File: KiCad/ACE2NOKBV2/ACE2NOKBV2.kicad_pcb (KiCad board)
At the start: 2 copper layers, 160 x 100 mm, 107 parts, among them IC1 78T, IC2 74367N, Q1 2N3904, Q2 2N3904, Q3 BC237, X1 6.556MHz

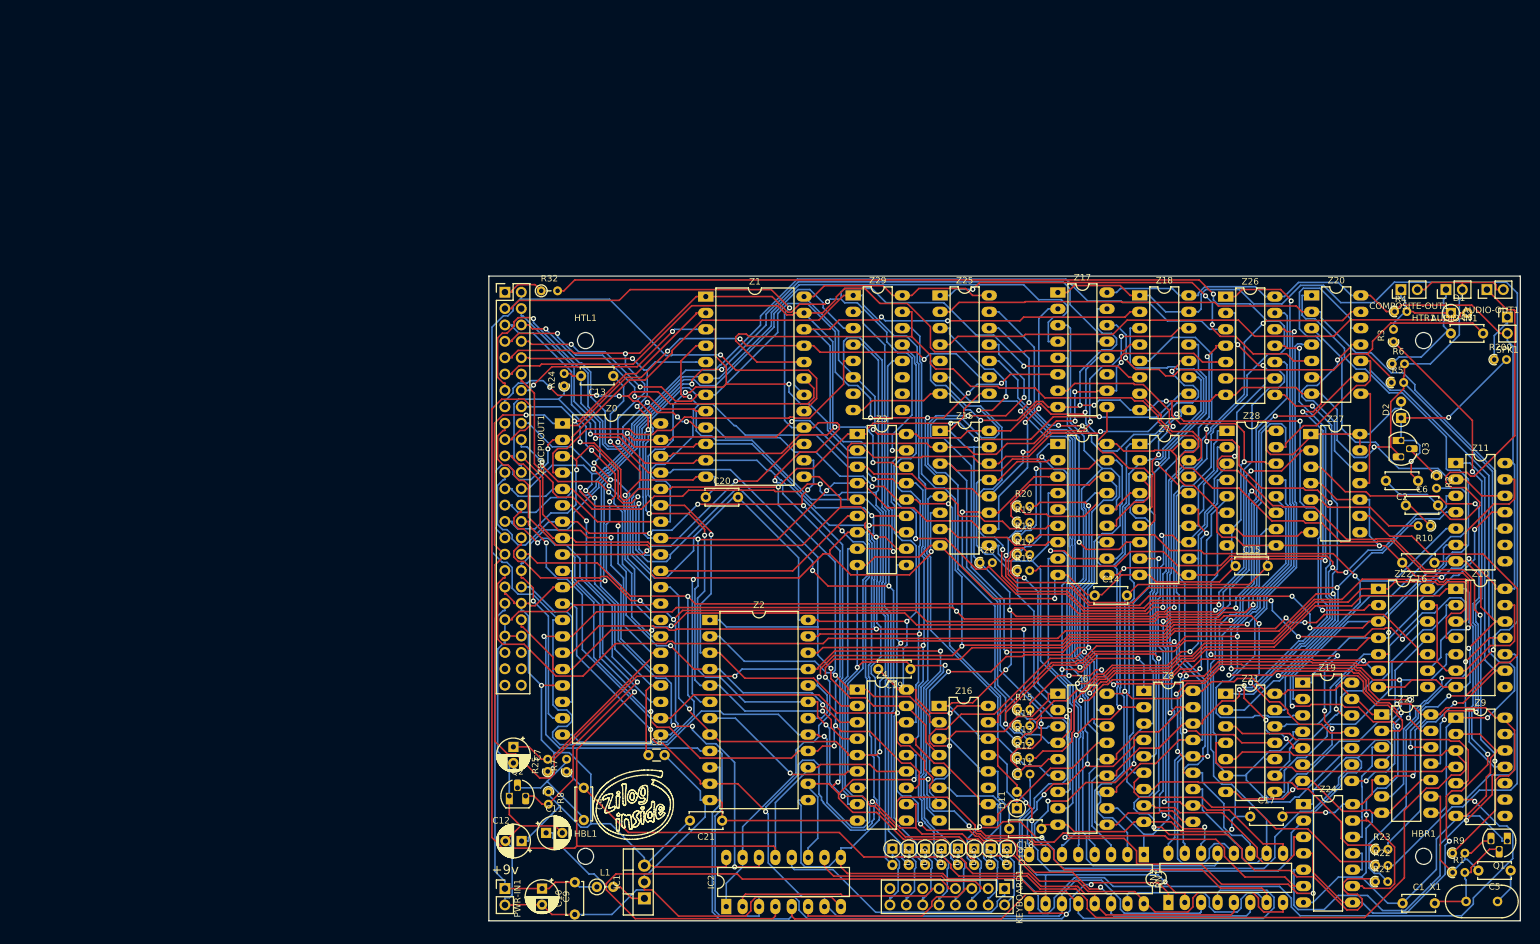
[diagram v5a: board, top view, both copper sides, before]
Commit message: Remove Speakrer leave 2 pin connector add single transistor amp to composite out.
Signed-off-by: John Bradley <flypie@rocketmail.com>
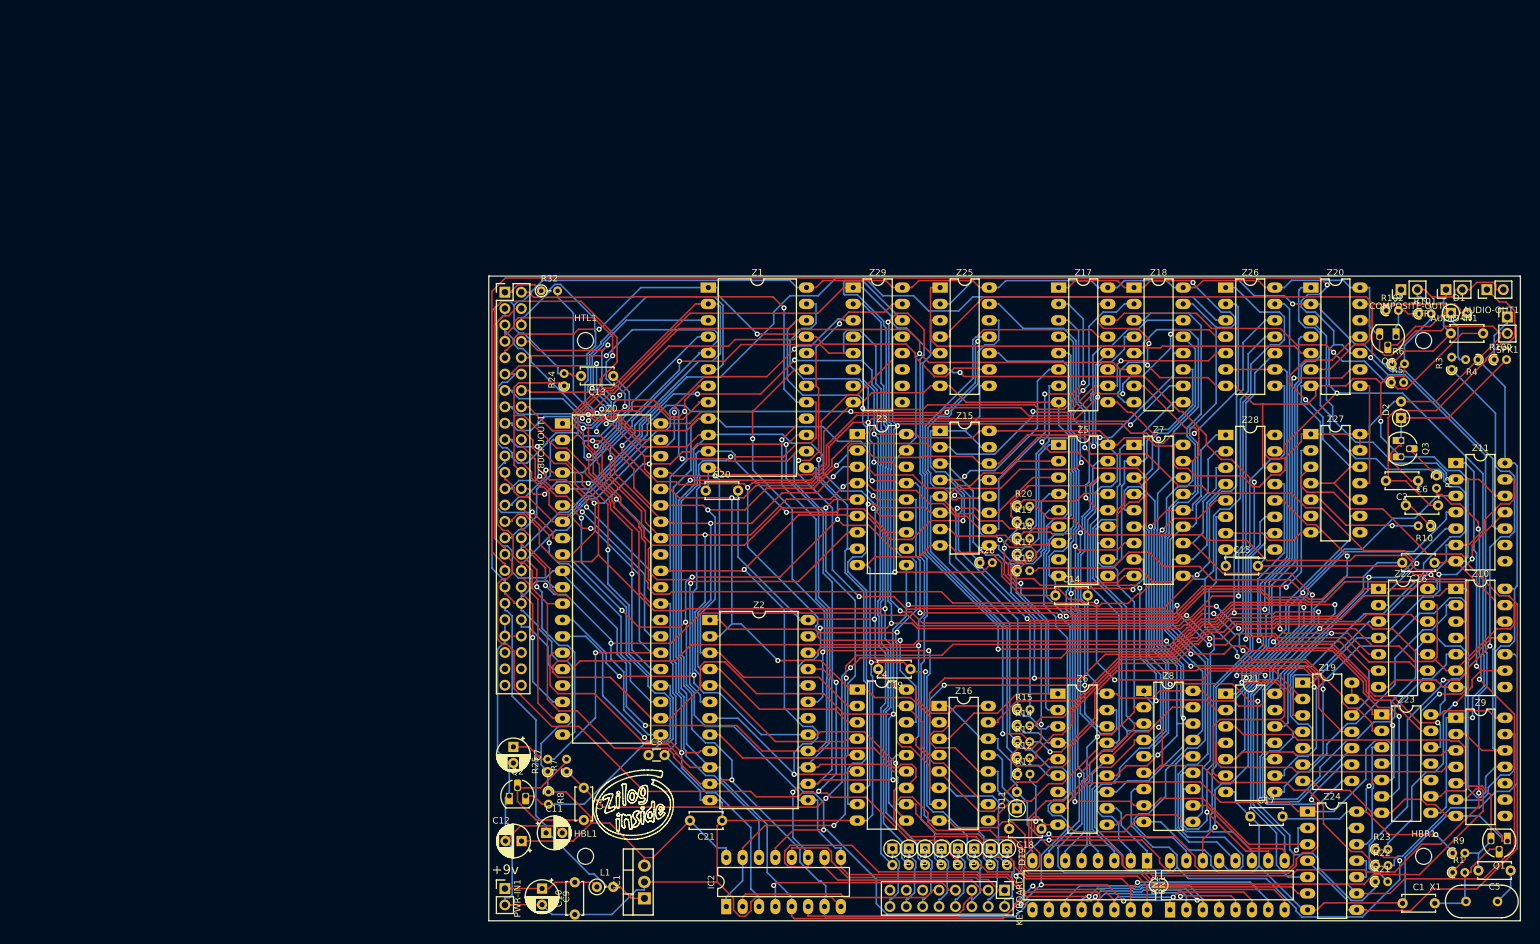
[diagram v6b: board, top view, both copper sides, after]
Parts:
- added Q4: 2N3904, Package_TO_SOT_THT:TO-92L_HandSolder, F.Cu at (211.8, 48.8)
- added R101: 100, Resistor_THT:R_Axial_DIN0204_L3.6mm_D1.6mm_P1.90mm_Vertical, F.Cu at (215.4, 45.2)
- added R102: 18, Resistor_THT:R_Axial_DIN0204_L3.6mm_D1.6mm_P1.90mm_Vertical, F.Cu at (210.3, 44.7)
- moved R4 14.9 mm to (224.5, 52.3), turned to 180 degrees
- moved R3 10.00 mm to (220.5, 53.8)
- moved C14 6.10 mm to (159.0, 88.9)
- moved C15 1.52 mm to (185.4, 84.3)
- moved Z18 1.51 mm to (171.2, 41.1)
- moved Z1 1.45 mm to (105.2, 41.1)
- moved Z26 1.40 mm to (185.4, 41.1)
- moved Z24 1.31 mm to (198.1, 122.4)
- moved Z20 1.23 mm to (198.6, 41.1)
- moved Z25 1.22 mm to (141.1, 41.1)
- moved Z29 1.22 mm to (127.6, 41.1)
- moved RN2 1.17 mm to (176.8, 137.7)
- moved RN1 1.08 mm to (173.2, 130.0)
- moved C20 1.02 mm to (104.8, 72.6)
- moved Z7 0.90 mm to (171.2, 65.5)
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- renumbered R200 to R100
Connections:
- net //BUSAK renamed /~BUSAK
- net //BUSRQ renamed /~BUSRQ
- net //HALT renamed /~HALT
- net //INT renamed /~INT
- net //IOREQ renamed /~IOREQ
- net //M1 renamed /~M1
- net //MREQ renamed /~MREQ
- net //RD renamed /~RD
- net //REFSH renamed /~REFSH
- net //VHOLD renamed /~VHOLD
- net //WAIT renamed /~WAIT
- net //WR renamed /~WR
- COMPOSITE-OUT1 pad 1: /VIDEO -> Net-(COMPOSITE-OUT1-Pad1)
- Z80CPUOUT1 pad 39: +9V -> +9Vsm
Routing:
- net /DA5: track 332.4 -> 244.2 mm, vias 5 -> 7
- net #NMI: track 883.2 -> 952.5 mm, vias 15 -> 6
- net /DA1: track 330.6 -> 269.3 mm, vias 5 -> 3
- net Net-(Z24-Pad5): track 159.1 -> 102.6 mm, vias 4 -> 2
- net Net-(IC2-Pad4): track 86.6 -> 32.4 mm, vias 0 -> 1
- net Net-(R23-Pad1): track 125.8 -> 179.3 mm, vias 1 -> 2
- net /CNT14: track 99.1 -> 146.2 mm, vias 1 -> 2
- net +9V: track 60.7 -> 15.0 mm
- net /DA6: track 309.9 -> 266.4 mm, vias 7 -> 3
- net Net-(RN1-Pad1): track 115.6 -> 158.8 mm, vias 1 -> 2
- net /CNT5: track 226.0 -> 183.0 mm
- net GND: track 896.5 -> 937.9 mm, vias 14 -> 6
- net +9Vsm: track 20.0 -> 58.1 mm
- net /A1: track 264.1 -> 228.1 mm, vias 8 -> 7
- net /A2: track 296.4 -> 263.4 mm, vias 4 -> 6
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
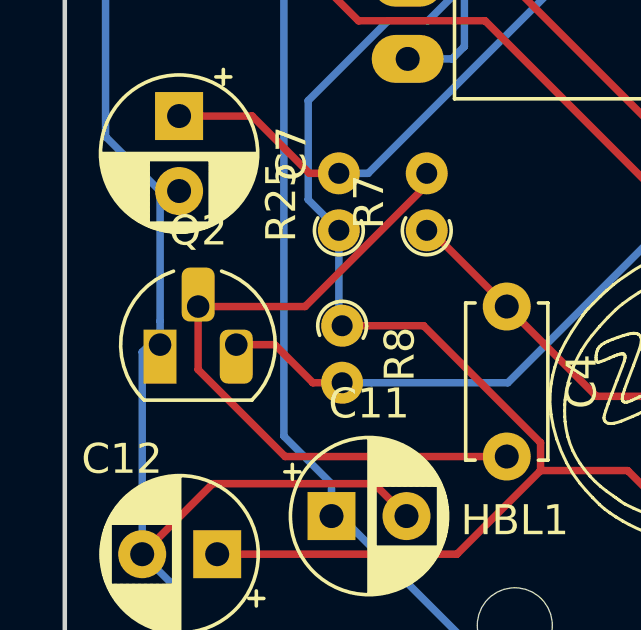
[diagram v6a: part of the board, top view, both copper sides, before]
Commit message: Correct transistor selection.
Signed-off-by: John Bradley <flypie@rocketmail.com>
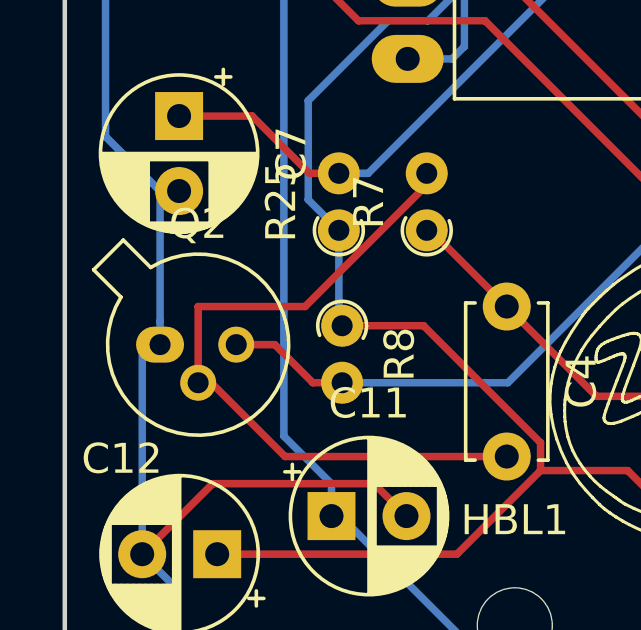
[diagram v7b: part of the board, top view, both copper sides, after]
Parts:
- Q2: value 2N3904 -> 2N2369; footprint Package_TO_SOT_THT:TO-92L_HandSolder -> Package_TO_SOT_THT:TO-18-3
- Q3: value BC237 -> BC183
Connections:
- net #CPUCLK renamed ~CPUCLK
- net #NMI renamed +5V
- net #RESET renamed ~RESET
- net /#WE renamed /~WE
- Q3 pad 1: Net-(C2-Pad1) -> GND
- Q3 pad 3: GND -> Net-(C2-Pad1)

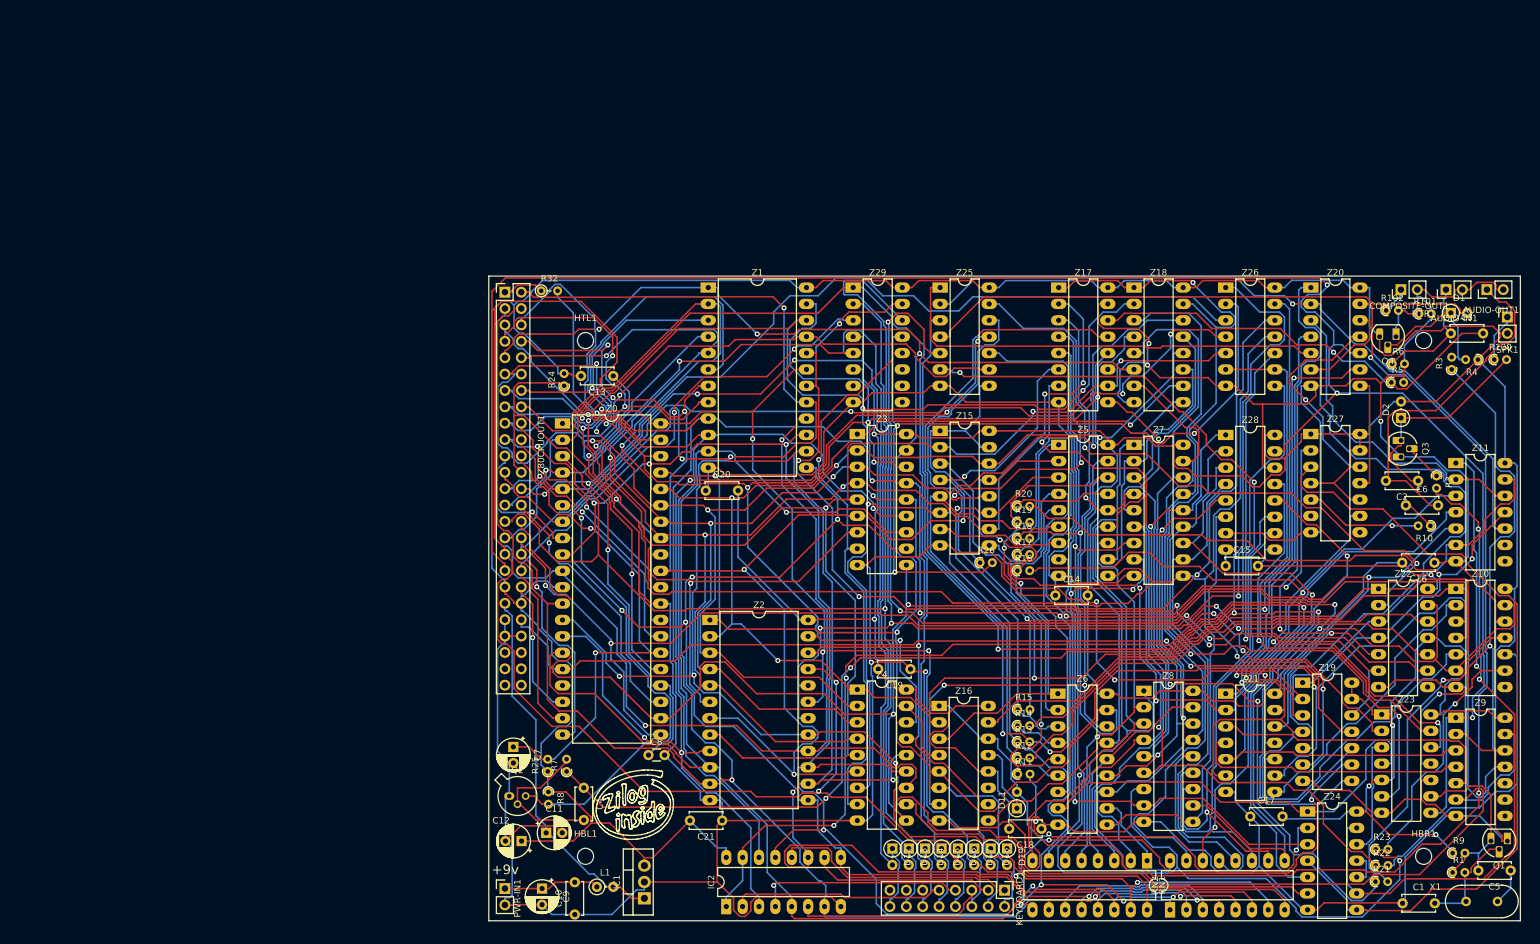
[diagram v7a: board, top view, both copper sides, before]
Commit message: Add enlarged power supply lines and place trim on Composite output.
Signed-off-by: John Bradley <flypie@rocketmail.com>
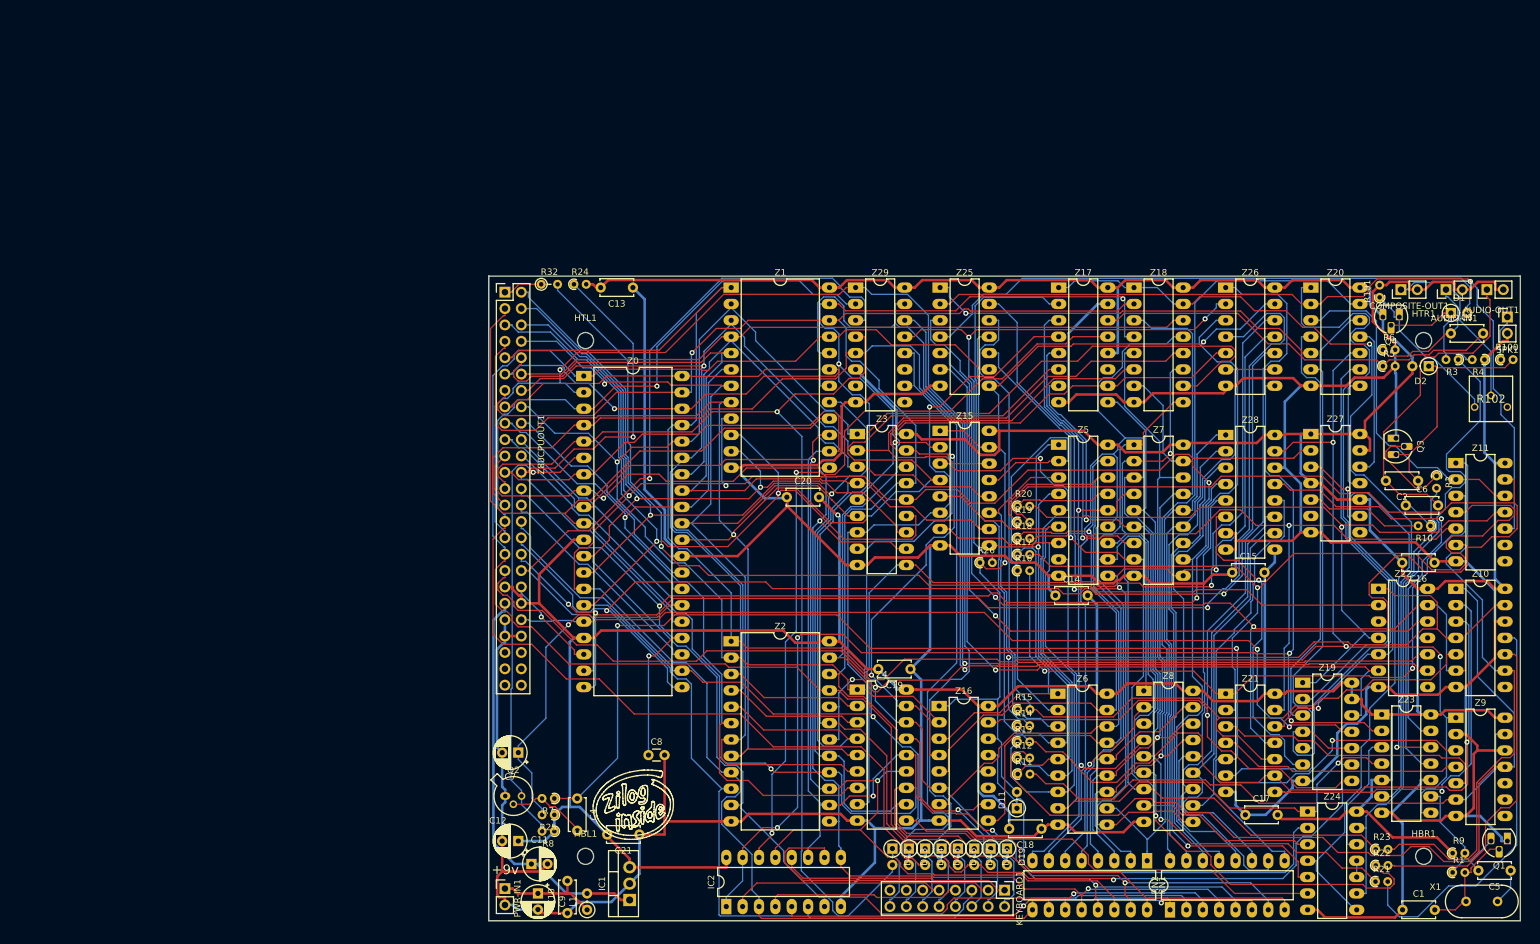
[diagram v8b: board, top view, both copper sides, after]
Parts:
- R102: value 18 -> 100; footprint Resistor_THT:R_Axial_DIN0204_L3.6mm_D1.6mm_P1.90mm_Vertical -> SamacSys_Parts:3362H1103LF
- moved R102 21.3 mm to (226.6, 58.4)
- moved R24 15.8 mm to (84.3, 40.6), turned to 0 degrees
- moved C13 14.1 mm to (93.5, 41.1)
- moved C21 13.0 mm to (94.5, 126.0)
- moved C20 12.6 mm to (117.3, 73.7)
- moved D2 9.11 mm to (216.9, 53.3), turned to 180 degrees
- moved Z0 8.07 mm to (85.9, 54.9)
- moved R25 6.81 mm to (81.3, 122.9), turned to 180 degrees
- moved R101 6.61 mm to (209.3, 42.7), turned to 90 degrees
- moved R8 6.16 mm to (81.3, 125.5), turned to 180 degrees
- moved C11 5.34 mm to (77.7, 130.6)
- moved Z2 4.67 mm to (108.7, 96.0)
- moved R7 4.60 mm to (81.3, 120.4), turned to 180 degrees
- moved L1 3.87 mm to (86.4, 137.7), turned to 90 degrees
- moved Z1 3.56 mm to (108.7, 41.1)
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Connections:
- R102 pad 1: Net-(COMPOSITE-OUT1-Pad1) -> Net-(Q4-Pad1)
- R102 pad 2: Net-(Q4-Pad1) -> Net-(COMPOSITE-OUT1-Pad1)
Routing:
- net +5V: track 952.5 -> 792.2 mm, vias 6 -> 1
- net GND: track 937.9 -> 827.7 mm, vias 6 -> 0
- net /DA0: track 391.2 -> 319.3 mm, vias 10 -> 2
- net /A11: track 287.2 -> 222.6 mm, vias 3 -> 0
- net Net-(RN1-Pad7): track 105.8 -> 166.8 mm, vias 1 -> 0
- net Net-(R23-Pad1): track 179.3 -> 123.0 mm, vias 2 -> 1
- net /CNT7: track 211.0 -> 154.8 mm, vias 1 -> 0
- net ~CPUCLK: track 304.0 -> 249.0 mm
- net Net-(D11-Pad2): track 257.2 -> 204.2 mm, vias 4 -> 2
- net /CNT14: track 146.2 -> 101.2 mm, vias 2 -> 1
- net /DA2: track 291.5 -> 248.4 mm, vias 2 -> 3
- net Net-(Z24-Pad4): track 123.6 -> 84.6 mm, vias 0 -> 1
- net /A8: track 270.4 -> 233.2 mm, vias 7 -> 4
- net Net-(R26-Pad2): track 127.0 -> 90.1 mm, vias 3 -> 2
- net Net-(Z19-Pad5): track 111.2 -> 76.7 mm
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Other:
- net class Default: trace_width 0.25 -> 0.2
- net class Power added: clearance 0.1524, trace_width 0.4, via_dia 0.8, via_drill 0.4
